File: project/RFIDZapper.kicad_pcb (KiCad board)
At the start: 2 copper layers, 29 parts, among them Q1 BC549, Q2 P3NB90 FP, Q3 BC549, Q4 IRF9630G, U1 NE555, U2 L7805, U3 TL071

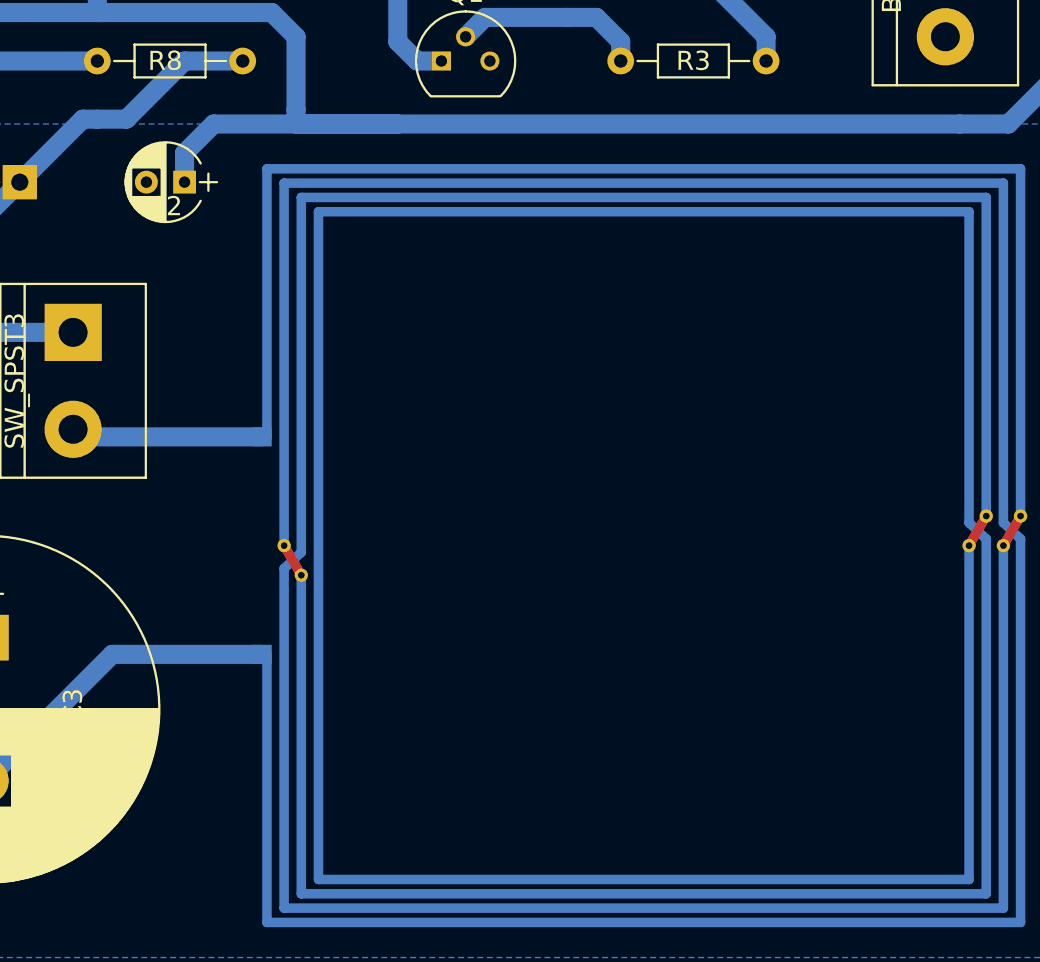
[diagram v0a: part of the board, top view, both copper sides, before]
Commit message: Added logos
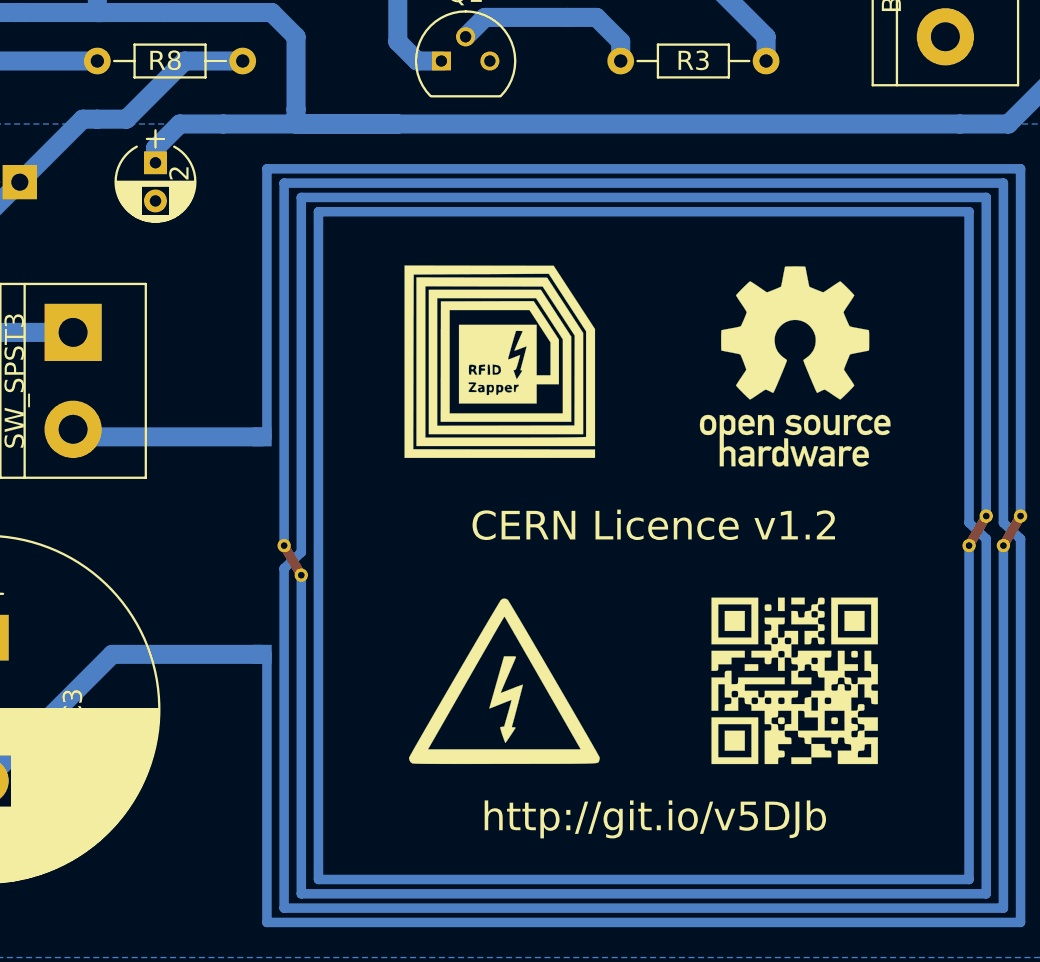
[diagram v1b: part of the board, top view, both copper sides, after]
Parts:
- added G***: LOGO, Graphics:open-source-hardware, F.Cu at (196.1, 102.9)
- added G***: LOGO, Graphics:high-voltaje, F.Cu at (180.8, 119.4)
- added G***: LOGO, Graphics:rfidzapper, F.Cu at (180.6, 102.6)
- added G***: LOGO, Graphics:gitqrcode, F.Cu at (196.1, 119.4)
- moved C2 1.83 mm to (162.6, 92.2), turned to 270 degrees
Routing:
- net Net-(C2-Pad1): track 146.3 -> 147.0 mm
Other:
- board text added: "CERN Licence v1.2"
- board text added: "http://git.io/v5DJb"

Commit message: Better 3D
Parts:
- R2: footprint Potentiometers:Potentiometer_Trimmer_Bourns_3266Y -> Potentiometers:Potentiometer_Trimmer_Bourns_3296W
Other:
- net class Default: trace_width 1 -> 0.25
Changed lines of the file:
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@@
   )
   (setup
-    (last_trace_width 1)
+    (last_trace_width 0.25)
     (trace_clearance 0.5)
     (zone_clearance 0.508)
@@
   (net_class Default "This is the default net class."
     (clearance 0.5)
-    (trace_width 1)
+    (trace_width 0.25)
     (via_dia 0.8)
     (via_drill 0.4)
@@
     (add_net "Net-(U3-Pad8)")
     (add_net Q)
+  )
+  (module Potentiometers:Potentiometer_Trimmer_Bourns_3296W (layer F.Cu)
+    (at 179.07 79.756 270)
+    (descr "Spindle Trimmer Potentiometer, Bourns 3296W, https://www.bourns.com/pdfs/3296.pdf")
+    (tags "Spindle Trimmer Potentiometer   Bourns 3296W")
+    (fp_text reference R2 (at -2.54 -3.66 270) (layer F.SilkS)
+      (effects (font (size 1 1) (thickness 0.15)))
+    )
+    (fp_text value 2k (at -2.54 3.67 270) (layer F.Fab)
+      (effects (font (size 1 1) (thickness 0.15)))
+    )
+    (fp_arc (start 0.955 1.15) (end 0.955 2.305) (angle -182) (layer F.SilkS) (width 0.12))
+    (fp_arc (start 0.955 1.15) (end -0.174 0.91) (angle -103) (layer F.SilkS) (width 0.12))
+    (fp_circle (center 0.955 1.15) (end 2.05 1.15) (layer F.Fab) (width 0.1))
+    (fp_line (start -7.305 -2.41) (end -7.305 2.42) (layer F.Fab) (width 0.1))
+    (fp_line (start -7.305 2.42) (end 2.225 2.42) (layer F.Fab) (width 0.1))
+    (fp_line (start 2.225 2.42) (end 2.225 -2.41) (layer F.Fab) (width 0.1))
+    (fp_line (start 2.225 -2.41) (end -7.305 -2.41) (layer F.Fab) (width 0.1))
+    (fp_line (start 1.786 0.454) (end 0.259 1.981) (layer F.Fab) (width 0.1))
+    (fp_line (start 1.652 0.32) (end 0.125 1.847) (layer F.Fab) (width 0.1))
+    (fp_line (start -7.365 -2.47) (end 2.285 -2.47) (layer F.SilkS) (width 0.12))
+    (fp_line (start -7.365 2.481) (end 2.285 2.481) (layer F.SilkS) (width 0.12))
+    (fp_line (start -7.365 -2.47) (end -7.365 2.481) (layer F.SilkS) (width 0.12))
+    (fp_line (start 2.285 -2.47) (end 2.285 2.481) (layer F.SilkS) (width 0.12))
+    (fp_line (start 1.831 0.416) (end 0.22 2.026) (layer F.SilkS) (width 0.12))
+    (fp_line (start 1.691 0.275) (end 0.079 1.885) (layer F.SilkS) (width 0.12))
+    (fp_line (start -7.6 -2.7) (end -7.6 2.7) (layer F.CrtYd) (width 0.05))
+    (fp_line (start -7.6 2.7) (end 2.5 2.7) (layer F.CrtYd) (width 0.05))
+    (fp_line (start 2.5 2.7) (end 2.5 -2.7) (layer F.CrtYd) (width 0.05))
+    (fp_line (start 2.5 -2.7) (end -7.6 -2.7) (layer F.CrtYd) (width 0.05))
+    (pad 1 thru_hole circle (at 0 0 270) (size 1.44 1.44) (drill 0.8) (layers *.Cu *.Mask)
+      (net 18 /THR))
+    (pad 2 thru_hole circle (at -2.54 0 270) (size 1.44 1.44) (drill 0.8) (layers *.Cu *.Mask)
+      (net 18 /THR))
+    (pad 3 thru_hole circle (at -5.08 0 270) (size 1.44 1.44) (drill 0.8) (layers *.Cu *.Mask)
+      (net 20 /DIS))
+    (model Potentiometers.3dshapes/Potentiometer_Trimmer_Bourns_3296W.wrl
+      (at (xyz 0 0 0))
+      (scale (xyz 1 1 1))
+      (rotate (xyz 0 0 -90))
+    )
   )
   (module RF_Modules:NFC_ANTENNA_40_40 (layer B.Cu)
@@
       (net 2 GNDPWR))
     (model ${KISYS3DMOD}/Connectors.3dshapes/bornier2.wrl
-      (at (xyz 0 0 0))
+      (at (xyz 0.09842519685039371 0 0))
       (scale (xyz 1 1 1))
       (rotate (xyz 0 0 0))
@@
     )
   )
-  (module Potentiometers:Potentiometer_Trimmer_Bourns_3266Y (layer F.Cu)
-    (at 179.07 79.756 270)
-    (descr "Spindle Trimmer Potentiometer, Bourns 3266Y, https://www.bourns.com/pdfs/3266.pdf")
-    (tags "Spindle Trimmer Potentiometer   Bourns 3266Y")
-    (fp_text reference R2 (at -2.54 -3.41 270) (layer F.SilkS)
-      (effects (font (size 1 1) (thickness 0.15)))
-    )
-    (fp_text value 2k (at -2.54 3.59 270) (layer F.Fab)
-      (effects (font (size 1 1) (thickness 0.15)))
-    )
-    (fp_line (start 1.1 -2.45) (end -6.15 -2.45) (layer F.CrtYd) (width 0.05))
-    (fp_line (start 1.1 2.6) (end 1.1 -2.45) (layer F.CrtYd) (width 0.05))
-    (fp_line (start -6.15 2.6) (end 1.1 2.6) (layer F.CrtYd) (width 0.05))
-    (fp_line (start -6.15 -2.45) (end -6.15 2.6) (layer F.CrtYd) (width 0.05))
-    (fp_line (start -0.37 0.92) (end -1.125 1.675) (layer F.SilkS) (width 0.12))
-    (fp_line (start -0.135 0.916) (end -1.009 1.791) (layer F.SilkS) (width 0.12))
-    (fp_line (start 0.875 0.466) (end 0.875 2.4) (layer F.SilkS) (width 0.12))
-    (fp_line (start 0.875 -2.22) (end 0.875 -0.465) (layer F.SilkS) (width 0.12))
-    (fp_line (start -5.955 0.466) (end -5.955 2.4) (layer F.SilkS) (width 0.12))
-    (fp_line (start -5.955 -2.22) (end -5.955 -0.465) (layer F.SilkS) (width 0.12))
-    (fp_line (start -5.955 2.4) (end 0.875 2.4) (layer F.SilkS) (width 0.12))
-    (fp_line (start -5.955 -2.22) (end 0.875 -2.22) (layer F.SilkS) (width 0.12))
-    (fp_line (start 0.162 0.396) (end -1.08 1.637) (layer F.Fab) (width 0.1))
-    (fp_line (start 0.27 0.504) (end -0.971 1.745) (layer F.Fab) (width 0.1))
-    (fp_line (start 0.815 -2.16) (end -5.895 -2.16) (layer F.Fab) (width 0.1))
-    (fp_line (start 0.815 2.34) (end 0.815 -2.16) (layer F.Fab) (width 0.1))
-    (fp_line (start -5.895 2.34) (end 0.815 2.34) (layer F.Fab) (width 0.1))
-    (fp_line (start -5.895 -2.16) (end -5.895 2.34) (layer F.Fab) (width 0.1))
-    (fp_circle (center -0.405 1.07) (end 0.485 1.07) (layer F.Fab) (width 0.1))
-    (fp_arc (start -0.405 1.07) (end -0.879 0.248) (angle -151) (layer F.SilkS) (width 0.12))
-    (fp_arc (start -0.405 1.07) (end -0.405 2.02) (angle -100) (layer F.SilkS) (width 0.12))
-    (pad 3 thru_hole circle (at -5.08 0 270) (size 1.44 1.44) (drill 0.8) (layers *.Cu *.Mask)
-      (net 20 /DIS))
-    (pad 2 thru_hole circle (at -2.54 0 270) (size 1.44 1.44) (drill 0.8) (layers *.Cu *.Mask)
-      (net 18 /THR))
-    (pad 1 thru_hole circle (at 0 0 270) (size 1.44 1.44) (drill 0.8) (layers *.Cu *.Mask)
-      (net 18 /THR))
-    (model Potentiometers.3dshapes/Potentiometer_Trimmer_Bourns_3266Y.wrl
-      (at (xyz 0 0 0))
-      (scale (xyz 0.393701 0.393701 0.393701))
-      (rotate (xyz 0 0 0))
-    )
-  )
   (module Resistors_ThroughHole:R_Axial_DIN0204_L3.6mm_D1.6mm_P7.62mm_Horizontal (layer F.Cu)
     (at 186.944 86.868)
@@
       (net 19 /VDD))
     (model ${KISYS3DMOD}/Connectors.3dshapes/bornier2.wrl
-      (at (xyz 0 0 0))
+      (at (xyz 0.09842519685039371 0 0))
       (scale (xyz 1 1 1))
       (rotate (xyz 0 0 0))
@@
       (net 2 GNDPWR))
     (model ${KISYS3DMOD}/Connectors.3dshapes/bornier2.wrl
-      (at (xyz 0 0 0))
+      (at (xyz 0.09842519685039371 0 0))
       (scale (xyz 1 1 1))
       (rotate (xyz 0 0 0))
@@
       (net 4 "Net-(C3-Pad1)"))
     (model ${KISYS3DMOD}/Connectors.3dshapes/bornier2.wrl
-      (at (xyz 0 0 0))
+      (at (xyz 0.09842519685039371 0 0))
       (scale (xyz 1 1 1))
       (rotate (xyz 0 0 0))
@@
     (pad 1 thru_hole circle (at 5.08 0 270) (size 1.99898 1.99898) (drill 1.00076) (layers *.Cu *.Mask)
       (net 5 "Net-(D1-Pad1)"))
+    (model ${KISYS3DMOD}/Choke_Toroid_ThroughHole.3dshapes/Choke_Toroid_15x40mm.wrl
+      (at (xyz 0.1968503937007874 0 0.1968503937007874))
+      (scale (xyz 1 1 1))
+      (rotate (xyz 90 90 0))
+    )
   )
   (module Housings_DIP:DIP-8_W7.62mm_LongPads (layer F.Cu)

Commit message: Lite routed
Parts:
- removed the G*** at (180.6, 102.6)
- added G***: LOGO, Graphics:ekoparty, F.Cu at (180.8, 101.6)

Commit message: Minor logos update
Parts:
- removed the G*** at (180.8, 101.6)
- added G***: LOGO, Graphics:rfidzapper, F.Cu at (180.8, 102.8)
- added G***: LOGO, Graphics:gitqrcode_cu, B.Cu at (180.8, 119.2)
- added G***: LOGO, Graphics:high-voltaje_cu, B.Cu at (196.0, 119.2)
- added G***: LOGO, Graphics:open-source-hardware_cu, B.Cu at (180.8, 103.0)
- added G***: LOGO, Graphics:rfidzapper_cu, B.Cu at (196.0, 102.8)
- moved G*** 0.16 mm to (180.8, 119.2)
- moved G*** 0.16 mm to (196.0, 119.2)
